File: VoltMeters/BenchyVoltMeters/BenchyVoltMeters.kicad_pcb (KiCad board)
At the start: 2 copper layers, 48 x 55 mm, 116 parts, among them J1 POWER CONN, J2 DSUB-26, J3 MB-COMMS, U1 INA826AIDRGR, U10 AP3401, U11 APX321, U2 INA826AIDRGR, U3 INA826AIDRGR, U4 INA826AIDRGR, U5 INA826AIDRGR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

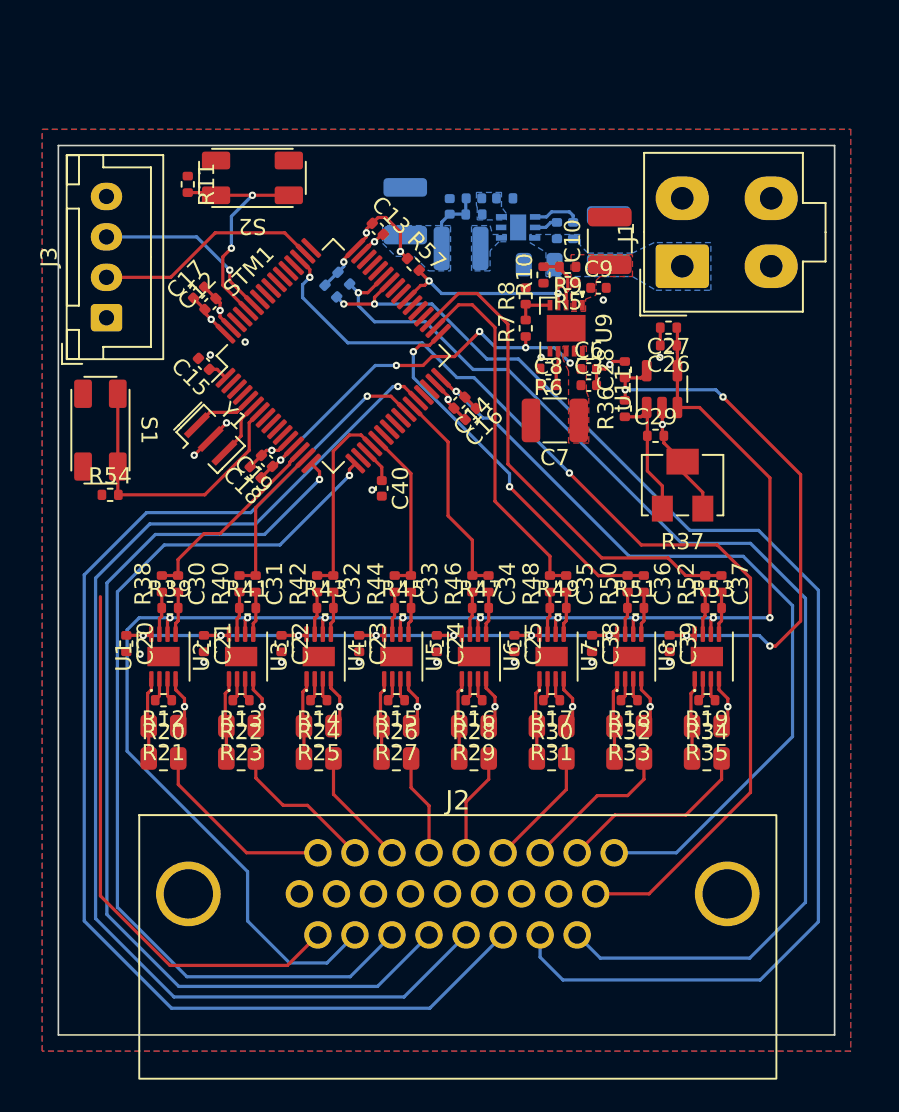
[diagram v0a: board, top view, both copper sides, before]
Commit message: Add voltmeter PCB
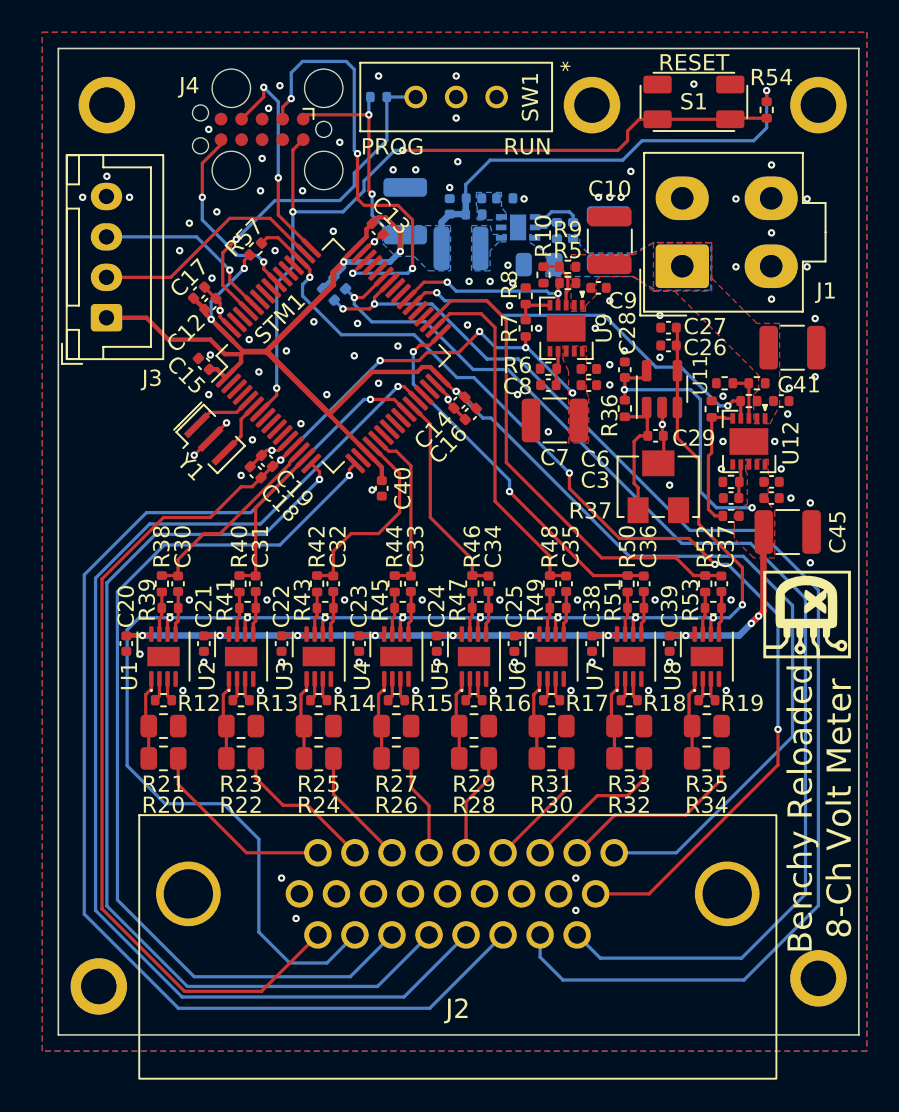
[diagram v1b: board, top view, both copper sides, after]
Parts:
- removed S2: BOOT0-SW, Daxxn_Switches:TL3365AF180QG
- added C41: 10uF, Capacitor_SMD:C_1210_3225Metric, F.Cu at (65.4, 32.5)
- added C42: 100nF, Capacitor_SMD:C_0402_1005Metric, F.Cu at (64.7, 35.8)
- added C43: 100nF, Capacitor_SMD:C_0402_1005Metric, F.Cu at (64.1, 41.8)
- added C44: 100nF, Capacitor_SMD:C_0402_1005Metric, F.Cu at (64.1, 40.8)
- added C45: 10uF, Capacitor_SMD:C_1210_3225Metric, F.Cu at (65.1, 43.9)
- added C46: 4.7uF, Capacitor_SMD:C_0402_1005Metric, F.Cu at (61.6, 41.8)
- added G***: LOGO, Daxxn_Logos_Art:Daxxn_Logo_S, F.Cu at (66.3, 49.0)
- added H1: M2, MountingHole:MountingHole_2.2mm_M2_ISO7380_Pad, F.Cu at (22.5, 72.0)
- added H2: M2, MountingHole:MountingHole_2.2mm_M2_ISO7380_Pad, F.Cu at (67.0, 71.5)
- added H3: M2, MountingHole:MountingHole_2.2mm_M2_ISO7380_Pad, F.Cu at (67.0, 17.5)
- added H4: M2, MountingHole:MountingHole_2.2mm_M2_ISO7380_Pad, F.Cu at (23.0, 17.5)
- added H5: M2, MountingHole:MountingHole_2.2mm_M2_ISO7380_Pad, F.Cu at (53.0, 17.5)
- added J4: SWD-TAG, Connector:Tag-Connect_TC2050-IDC-FP_2x05_P1.27mm_Vertical, F.Cu at (32.6, 19.0)
- added R58: 10K, Resistor_SMD:R_0402_1005Metric, F.Cu at (62.7, 35.8)
- added R59: 183.44K, Resistor_SMD:R_0402_1005Metric, F.Cu at (61.6, 42.9)
- added R60: 15K, Resistor_SMD:R_0402_1005Metric, F.Cu at (63.2, 34.7)
- added R61: 10K, Resistor_SMD:R_0402_1005Metric, F.Cu at (61.2, 34.7)
- added R62: 12.5K, Resistor_SMD:R_0402_1005Metric, F.Cu at (60.4, 36.3)
- added R63: 22.1K, Resistor_SMD:R_0402_1005Metric, F.Cu at (61.6, 40.8)
- added SW1: BOOT-SW, Daxxn_Switches:EG1218, F.Cu at (47.1, 17.0)
- added U12: TPS7A94, Daxxn_Packages:WSON-10-1EP_3x3mm, F.Cu at (62.7, 38.3)
- C20, C21, C22, C23, C24, C25, C26, C27, C28, C29, C30, C31, C32, C33, C34, C35, C36, C37, C38, C39: footprint Resistor_SMD:R_0402_1005Metric -> Capacitor_SMD:C_0402_1005Metric
- R11: moved to B.Cu
- moved R54 47.1 mm to (63.8, 17.8), turned to -90 degrees
- moved S1 41.9 mm to (59.3, 17.3), turned to 180 degrees
- moved R11 13.0 mm to (39.8, 17.0), turned to 0 degrees
- moved R57 9.80 mm to (32.2, 26.4), turned to 45 degrees
- moved R37 1.50 mm to (57.1, 41.1)
- moved R55 0.39 mm to (37.4, 28.5)
- moved R56 0.25 mm to (36.7, 29.2)
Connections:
- C20 pad 1: VDDA -> VCCA
- C21 pad 1: VDDA -> VCCA
- C22 pad 1: VDDA -> VCCA
- C23 pad 1: VDDA -> VCCA
- C24 pad 1: VDDA -> VCCA
- C25 pad 1: VDDA -> VCCA
- C28 pad 1: VDDA -> VCCA
- C38 pad 1: VDDA -> VCCA
- C39 pad 1: VDDA -> VCCA
- R36 pad 2: VDDA -> VCCA
- R57 pad 2: /MC/VDDA-PG -> /INT-CTRLS
- STM1 pad 38: unconnected-(STM1C-PC7-Pad38) -> /MC/VCCA-PG
- STM1 pad 46: unconnected-(STM1C-PA13-Pad46) -> /MC/SWDIO
- STM1 pad 49: unconnected-(STM1C-PA14-Pad49) -> /MC/SWCLK
- STM1 pad 55: unconnected-(STM1C-PB3-Pad55) -> /MC/SWTRACE
- U1 pad 8: VDDA -> VCCA
- U11 pad 5: VDDA -> VCCA
- U2 pad 8: VDDA -> VCCA
- U3 pad 8: VDDA -> VCCA
- U4 pad 8: VDDA -> VCCA
- U5 pad 8: VDDA -> VCCA
- U6 pad 8: VDDA -> VCCA
- U7 pad 8: VDDA -> VCCA
- U8 pad 8: VDDA -> VCCA
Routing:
- net VDD: track 71.2 -> 157.3 mm, vias 5 -> 8
- net VCCA: track 0.00 -> 74.8 mm, vias 0 -> 12
- net VDDA: track 139.4 -> 76.2 mm, vias 16 -> 5
- net GND: track 73.1 -> 39.0 mm, vias 30 -> 115
- net RESET: track 18.1 -> 50.4 mm, vias 0 -> 3
- net /MC/SWDIO: track 0.00 -> 27.6 mm, vias 0 -> 4
- net /MC/VCCA-PG: track 0.00 -> 24.7 mm, vias 0 -> 2
- net /MC/SWCLK: track 0.00 -> 13.7 mm, vias 0 -> 2
- net /MC/SWTRACE: track 0.00 -> 11.9 mm, vias 0 -> 2
- net Net-(U12-FB_PG): track 0.00 -> 8.16 mm
- net BOOT0: track 14.9 -> 22.2 mm, vias 2 -> 1
- net /INT-CTRLS: track 63.1 -> 67.8 mm, vias 2 -> 4
- net Net-(U12-EN_UV): track 0.00 -> 3.16 mm
- net Net-(U12-NR/SS): track 0.00 -> 2.12 mm
- net VREF: track 99.8 -> 98.2 mm
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- added copper zone on F.Cu, net VCCA
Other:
- board size 48 x 55 mm -> 49.5 x 61 mm
- board text added: "Benchy Reloaded 8-Ch Volt Meter"
- board text added: "PROG"
- board text added: "RESET"
- board text added: "RUN"

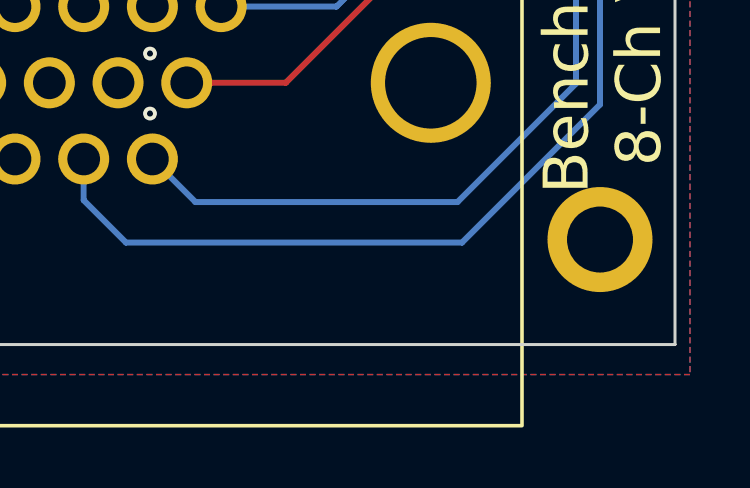
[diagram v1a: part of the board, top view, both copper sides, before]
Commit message: Wrap up REV2 and add voltmeter gerbers
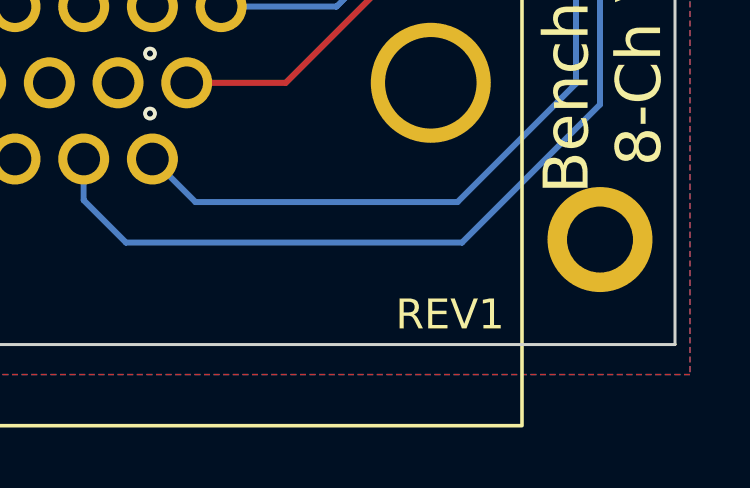
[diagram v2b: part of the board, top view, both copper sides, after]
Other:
- board text added: "REV1"
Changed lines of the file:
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@@
     (effects (font (size 1 1) (thickness 0.15)) (justify top))
+  )
+  (gr_text "REV1" (at 62 74) (layer "F.SilkS")
+    (effects (font (size 1 1) (thickness 0.15)))
   )
   (gr_text "Benchy Reloaded\n8-Ch Volt Meter" (at 67.1 61 90) (layer "F.SilkS")
